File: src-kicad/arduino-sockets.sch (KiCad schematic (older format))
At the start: 11 parts, among them U9 TXB0108

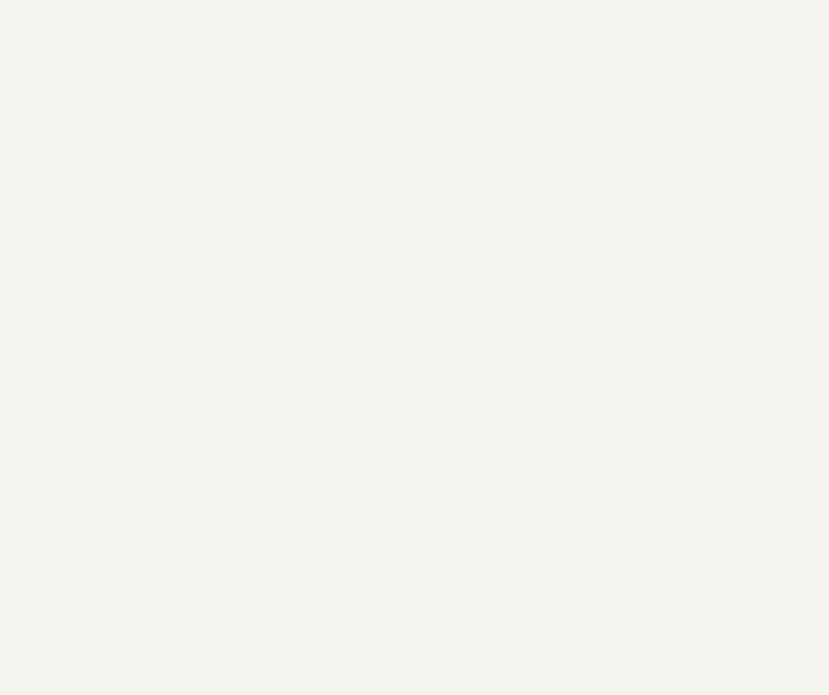
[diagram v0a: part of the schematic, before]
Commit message: Kicad migration: gpio D7-D0 connector
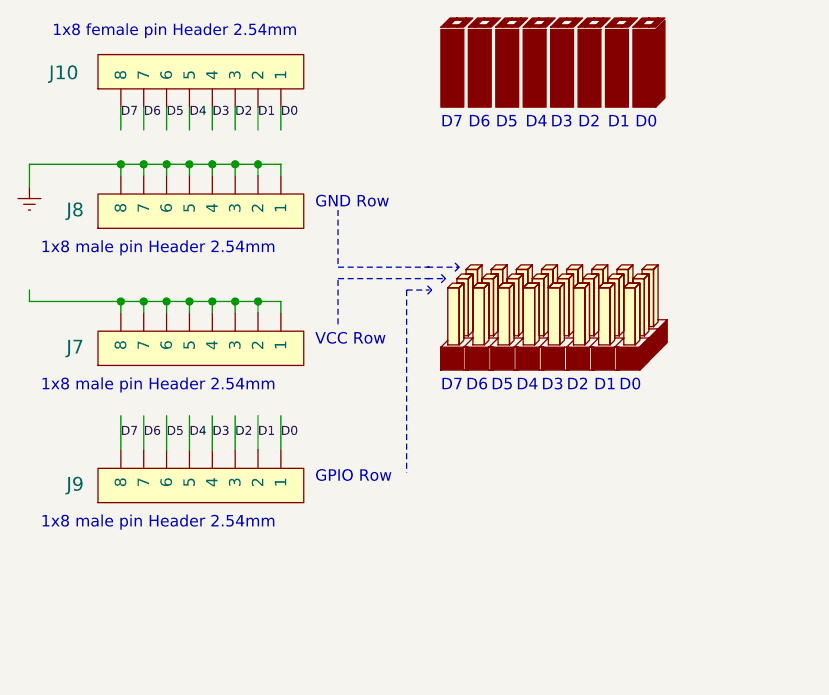
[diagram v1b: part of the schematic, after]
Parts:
- added J10: 1x8_female_pin_Header_2.54mm, symbol 1x8_female_pin_Header_2.54mm
- added J7, J8, J9: 1x8_male_pin_Header_2.54mm, symbol 1x8_male_pin_Header_2.54mm
- added doc1: 1x8_pin_female_header_DOC, symbol 1x8_pin_female_header_DOC
- added doc2: 3x8_pin_male_header_DOC, symbol 3x8_pin_male_header_DOC
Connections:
- wire segments 43 -> 79
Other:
- note added: "1x8 female pin Header 2.54mm"
- note added: "1x8 male pin Header 2.54mm"
- note added: "D0"
- note added: "D1"
- note added: "D2"
- note added: "D3"
- note added: "D4"
- note added: "D5"
- note added: "D6"
- note added: "D7"
- note added: "GND Row"
- note added: "GPIO Row"
- note added: "VCC Row"

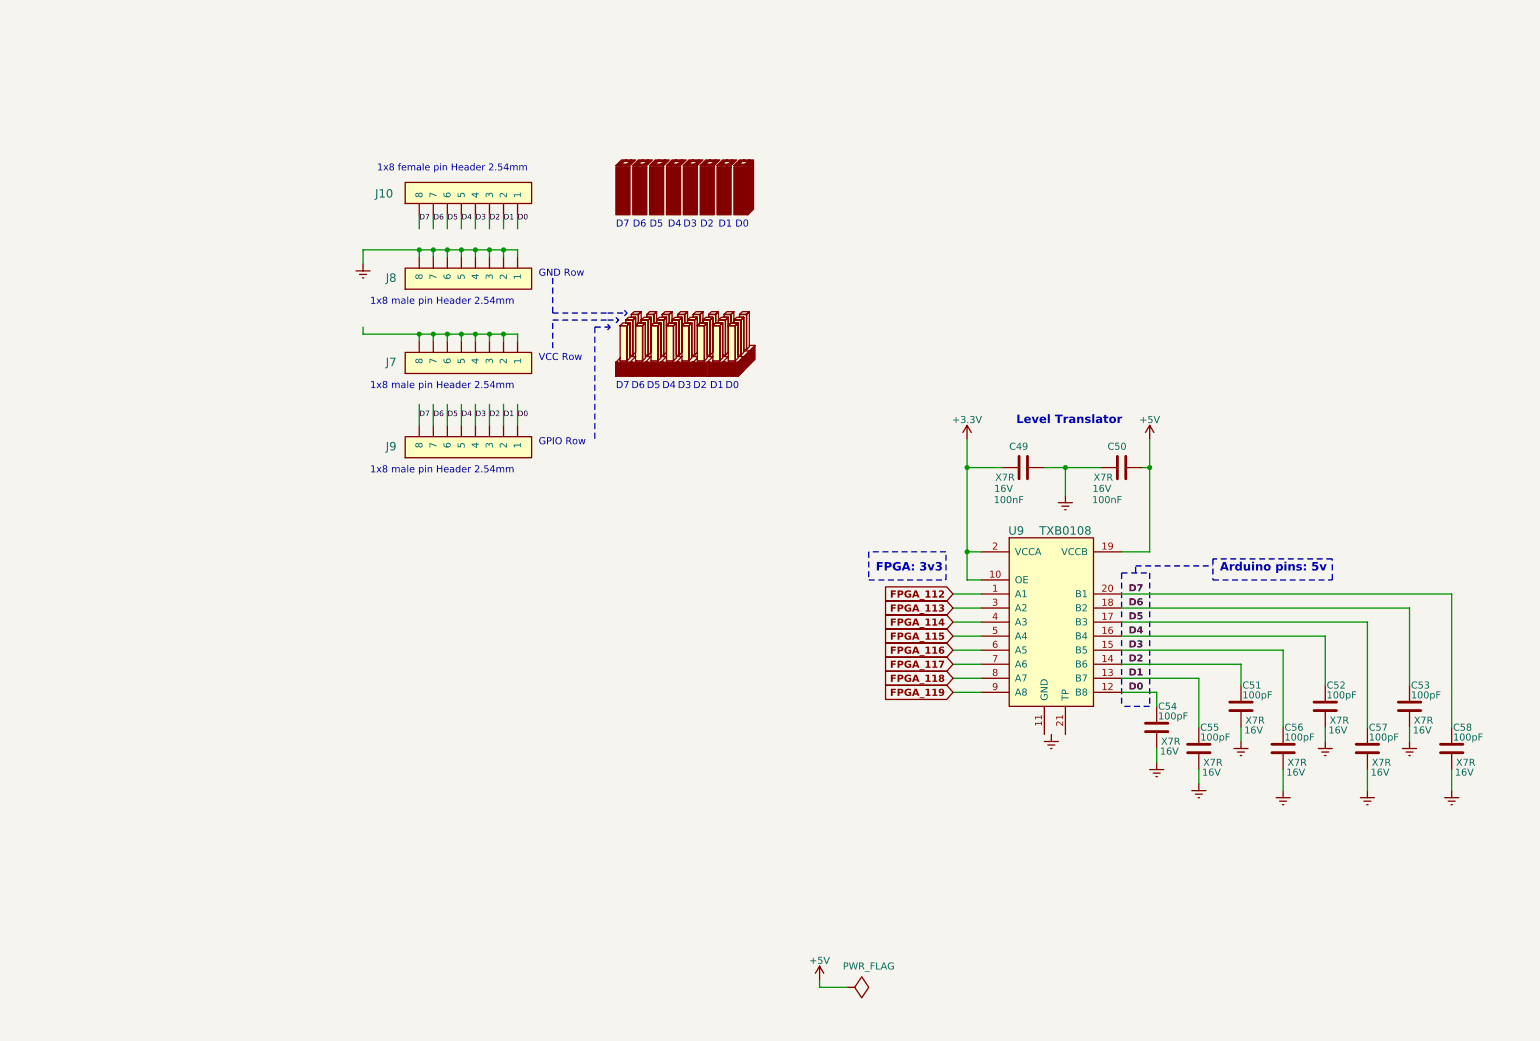
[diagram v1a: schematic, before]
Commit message: Kicad migration. Power supply sheet started
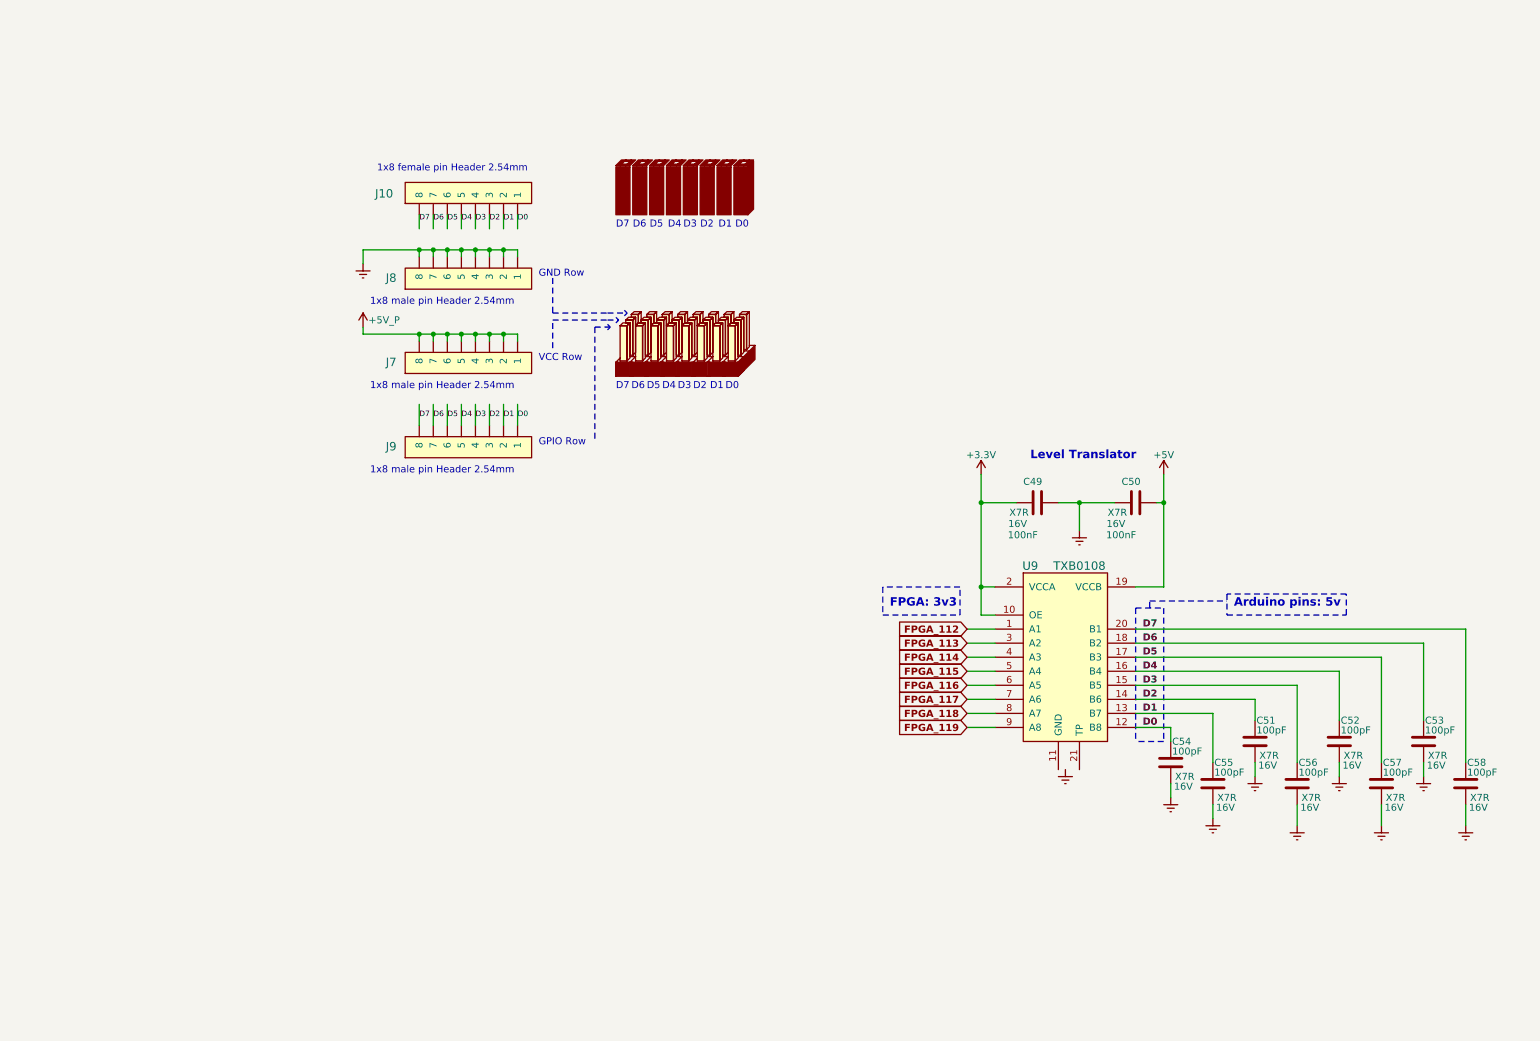
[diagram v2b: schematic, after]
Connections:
- net labels added: +5V_P
- wire segments 79 -> 77
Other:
- moved on the sheet: C49, C50, C51, C52, C53, C54, C55, C56, C57, C58, U9

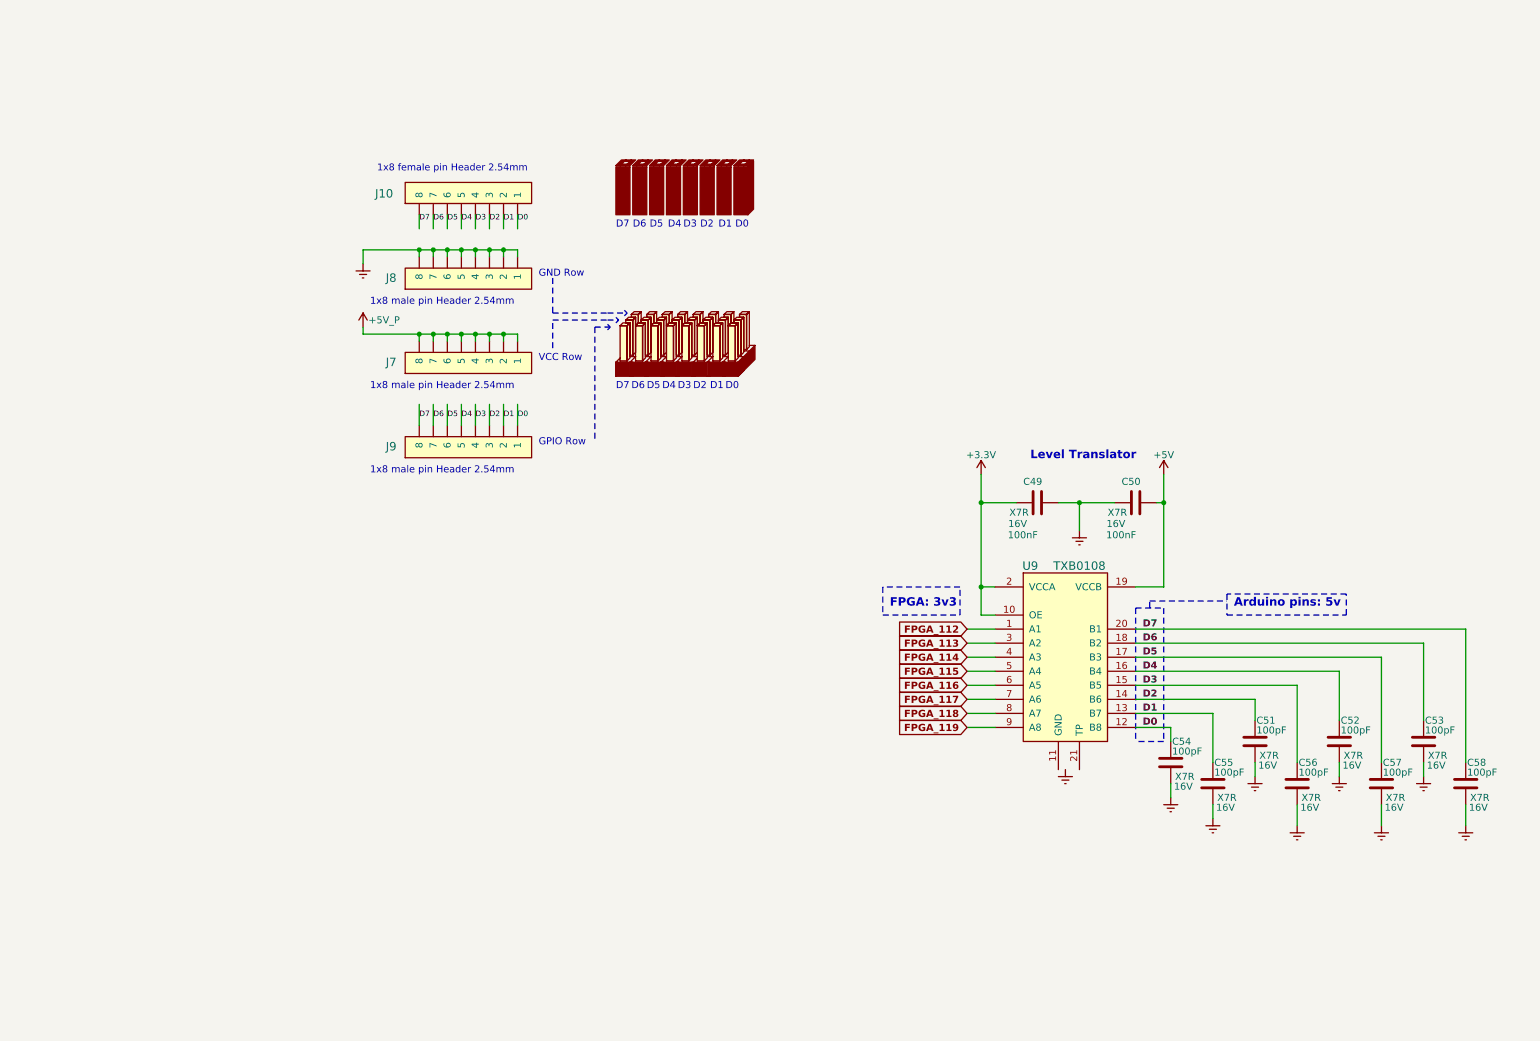
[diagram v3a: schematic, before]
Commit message: Kicad migration: All the arduino sockets placed
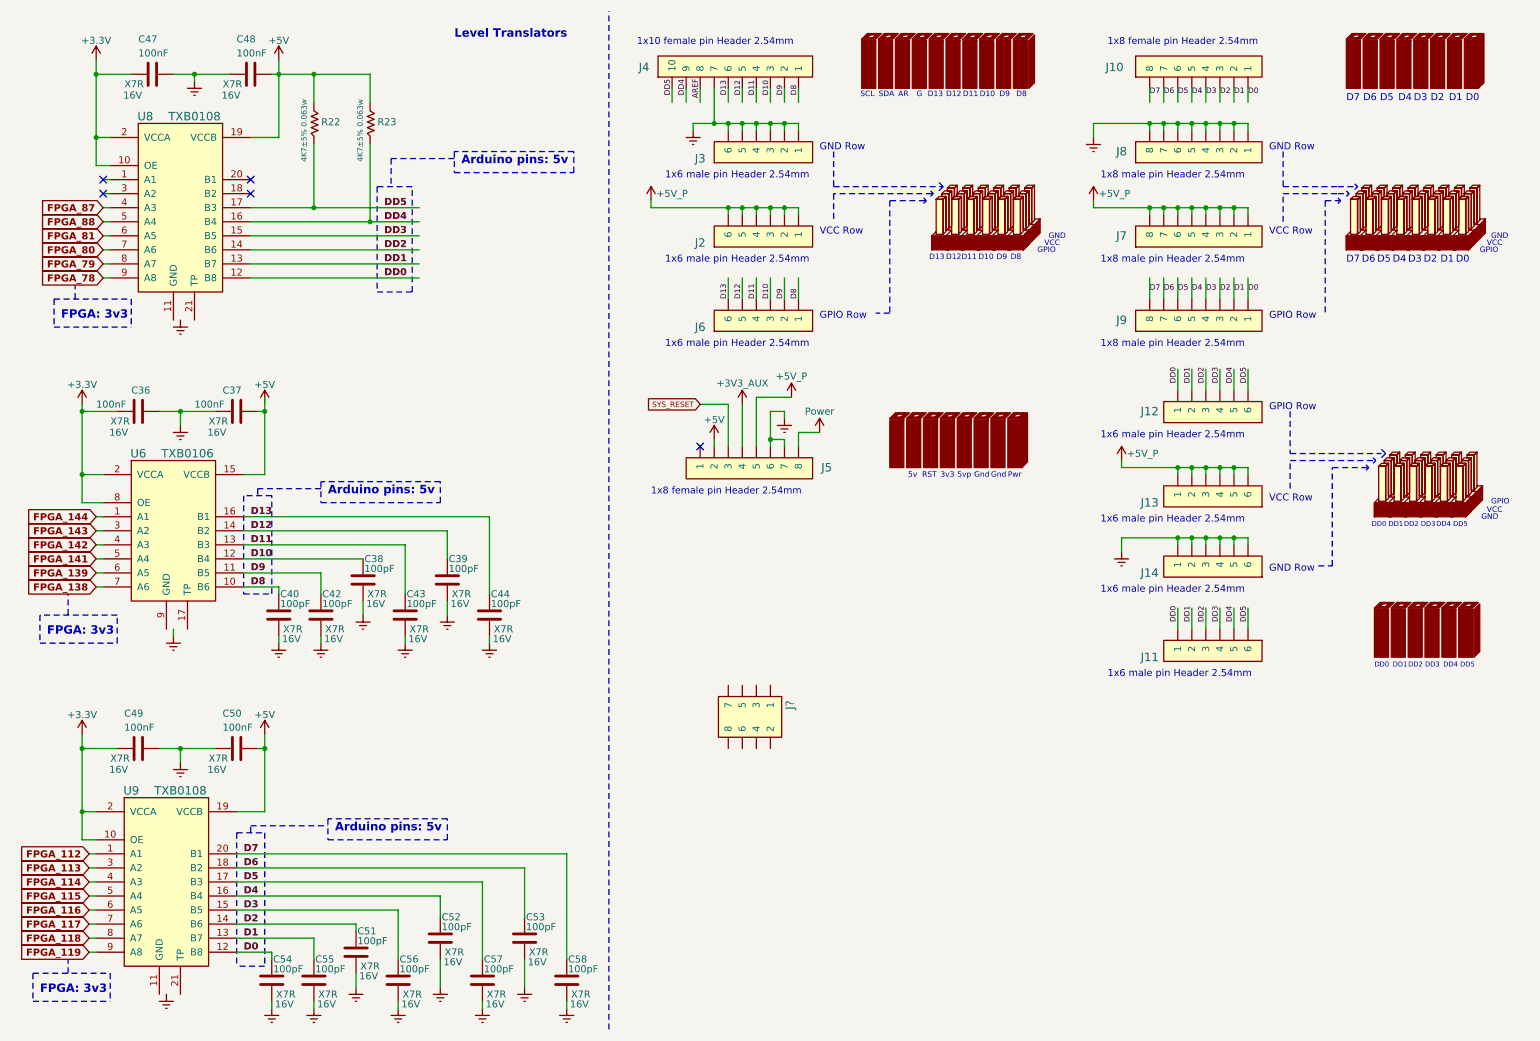
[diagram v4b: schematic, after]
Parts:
- added C36, C37, C47, C48: 100nF, symbol C
- added C38, C39, C40, C42, C43, C44: 100pF, symbol C
- added J11: 1x6_female_pin_Header_2.54mm, symbol 1x6_female_pin_Header_2.54mm
- added J12, J13, J14, J2, J3, J6: 1x6_male_pin_Header_2.54mm, symbol 1x6_male_pin_Header_2.54mm
- added J4: 1x10_female_pin_Header_2.54mm, symbol 1x10_female_pin_Header_2.54mm
- added J5: 1x8_female_pin_Header_2.54mm, symbol 1x8_female_pin_Header_2.54mm
- added J?: 2x4_male_pin_Header_2.54mm, symbol 2x4_male_pin_Header_2.54mm
- added R22, R23: 4K7±5% 0.063w, symbol R
- added U6: TXB0106, symbol TXB0106
- added U8: TXB0108, symbol TXB0108
- added doc3: 1x10_pin_female_header_DOC, symbol 1x10_pin_female_header_DOC
- added doc4, doc?: 3x6_pin_male_header_DOC, symbol 3x6_pin_male_header_DOC
- added doc?: 1x6_pin_female_header_DOC, symbol 1x6_pin_female_header_DOC
- added doc?: 1x8_pin_female_header_DOC, symbol 1x8_pin_female_header_DOC
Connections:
- net labels added: +3V3_AUX, AREF, D10, D11, D12, D13, D8, D9, DD0, DD1, DD2, DD3, DD4, DD5, FPGA_138, FPGA_139, FPGA_141, FPGA_142, FPGA_143, FPGA_144, FPGA_78, FPGA_79, FPGA_80, FPGA_81, FPGA_87, FPGA_88, Power, SYS_RESET
- wire segments 77 -> 210
- no-connect marks 0 -> 5
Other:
- note added: "1x10 female pin Header 2.54mm"
- note added: "1x6 male pin Header 2.54mm"
- note added: "3v3"
- note added: "5v"
- note added: "5vp"
- note added: "AR"
- note added: "D10"
- note added: "D11"
- note added: "D12"
- note added: "D13"
- note added: "D8"
- note added: "D9"
- note added: "DD0"
- note added: "DD1"
- note added: "DD2"
- note added: "DD3"
- note added: "DD4"
- note added: "DD5"
- note added: "G"
- note added: "GND"
- note added: "GPIO"
- note added: "Gnd"
- note added: "Level Translators"
- note added: "Pwr"
- note added: "RST"
- note added: "SCL"
- note added: "SDA"
- note added: "VCC"
- note removed: "Level Translator"
- moved on the sheet: C49, C50, C51, C52, C53, C54, C55, C56, C57, C58, J10, J7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

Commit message: kicad migration: arduino sockets sheet. More documentation
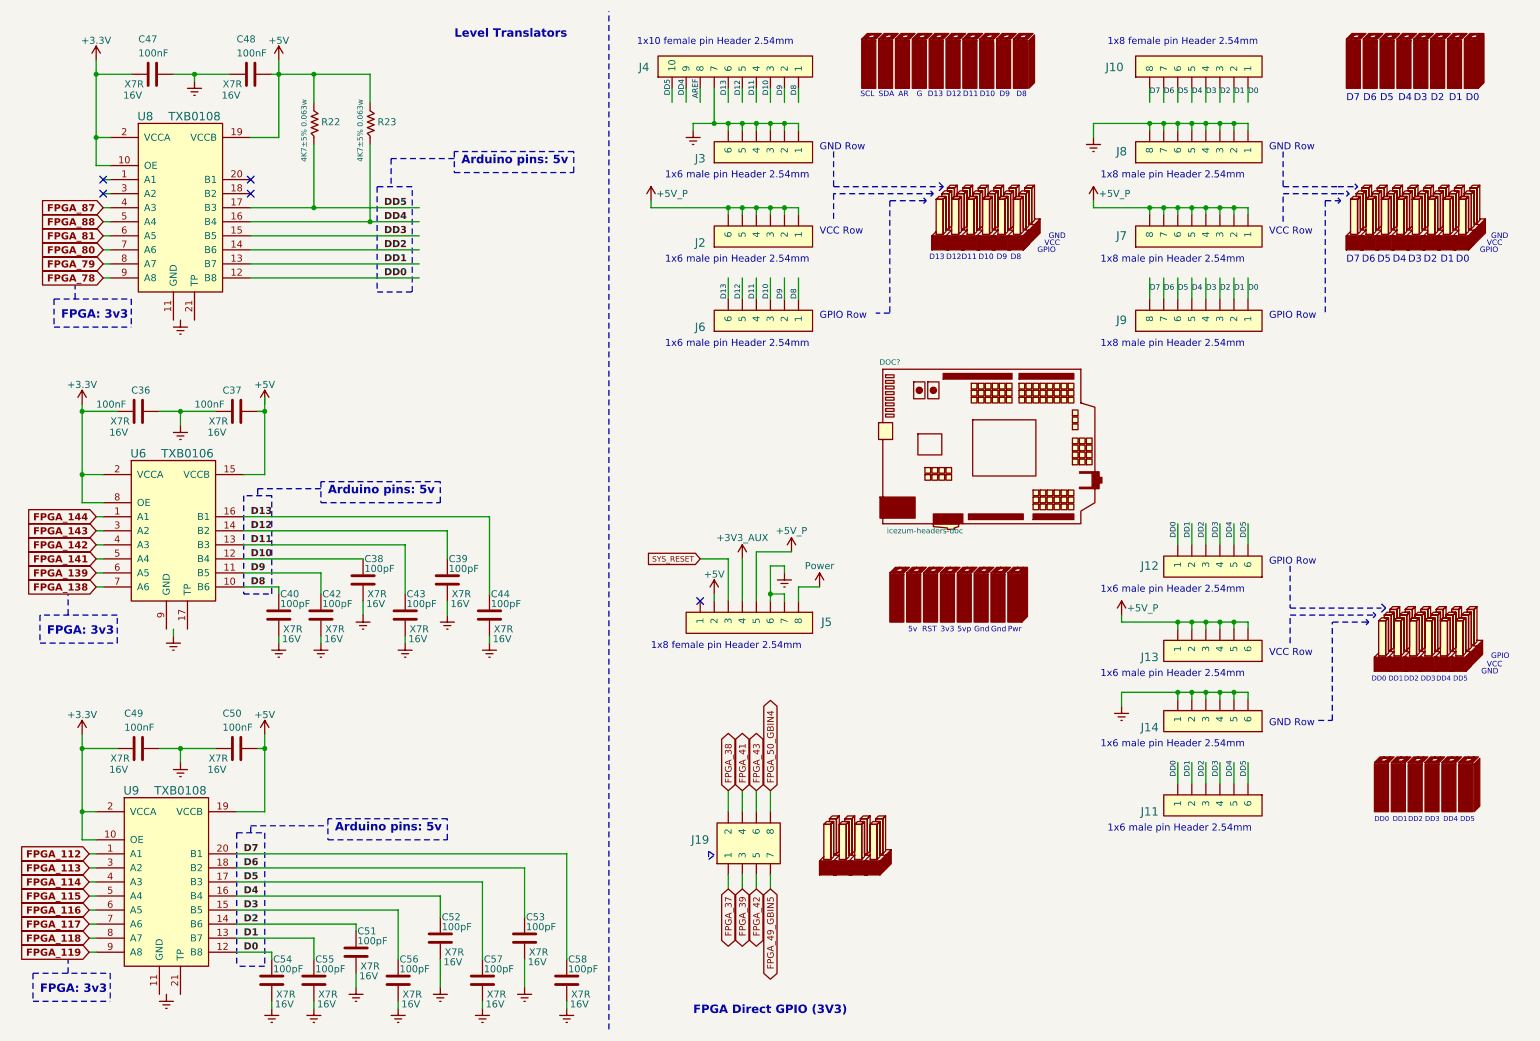
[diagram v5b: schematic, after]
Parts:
- added DOC?: icezum-headers-doc, symbol icezum-headers-doc
- added doc?: 2x4_pin_male_header_DOC, symbol 2x4_pin_male_header_DOC
- gave numbers to parts that had none: 1
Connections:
- net labels added: FPGA_37, FPGA_38, FPGA_39, FPGA_41, FPGA_42, FPGA_43, FPGA_49_GBIN5, FPGA_50_GBIN4
- wire segments 210 -> 218
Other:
- note added: "FPGA Direct GPIO (3V3)"
- moved on the sheet: J11, J12, J13, J14, J19, J5
